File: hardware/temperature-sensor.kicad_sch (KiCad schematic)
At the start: 35 parts, among them J1 USB_B, J2 Barrel_Jack, J3 Conn_01x02_Pin, J4 Conn_01x03, SW1 SW_Push, U1 MCP2221AxP, U2 MCP1702-3302E, U3 ESP-01v090, U4 AHT10

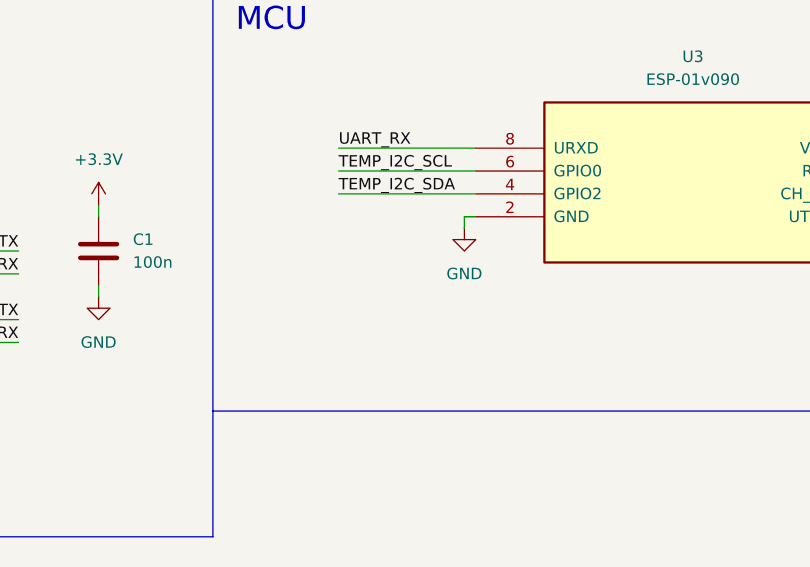
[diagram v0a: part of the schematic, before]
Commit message: Rev 0.2 - Added jumper to support UART boot
Signed-off-by: Matthew <mnickson@sidingsmedia.com>
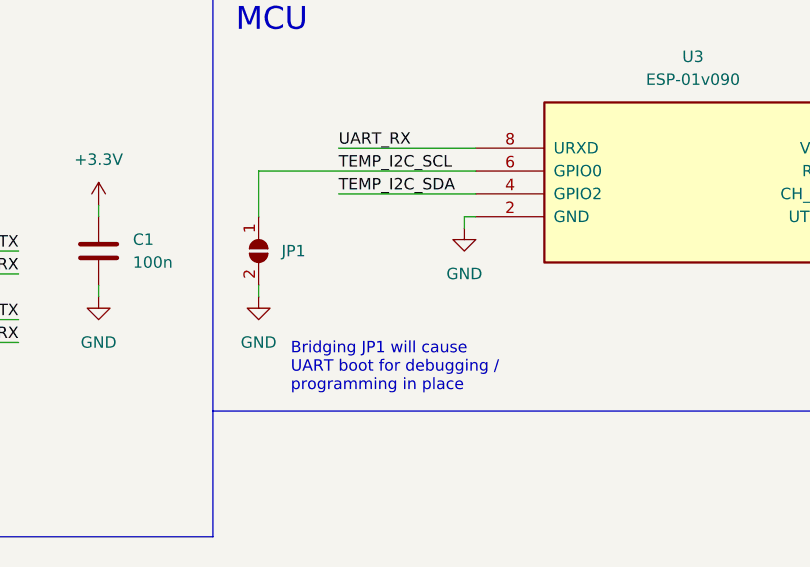
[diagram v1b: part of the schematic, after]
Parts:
- added JP1: SolderJumper_2_Open, Jumper:SolderJumper-2_P1.3mm_Open_Pad1.0x1.5mm, symbol Jumper:SolderJumper_2_Open
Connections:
- net GND: now also JP1.2 (B)
- net TEMP_I2C_SCL: now also JP1.1 (A)
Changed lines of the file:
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@@
   (title_block
     (title "Temperature Sensor")
-    (date "2024-01-07")
-    (rev "0.1")
+    (date "2024-01-13")
+    (rev "0.2")
     (company "Sidings Media")
     (comment 1 "Licence: CERN-OHL-P-2.0 or any later version")
@@
     (stroke (width 0) (type default))
   )
+  (wire (pts (xy 95.25 132.08) (xy 95.25 133.35))
+    (stroke (width 0) (type default))
+  )
   (wire (pts (xy 140.97 85.09) (xy 140.97 86.36))
     (stroke (width 0) (type default))
@@
     (stroke (width 0) (type default))
   )
-  (wire (pts (xy 104.14 119.38) (xy 119.38 119.38))
+  (wire (pts (xy 95.25 119.38) (xy 119.38 119.38))
     (stroke (width 0) (type default))
   )
@@
     (stroke (width 0) (type default))
   )
+  (wire (pts (xy 95.25 124.46) (xy 95.25 119.38))
+    (stroke (width 0) (type default))
+  )
   (wire (pts (xy 257.81 25.4) (xy 257.81 26.67))
     (stroke (width 0) (type default))
@@
   (wire (pts (xy 257.81 48.26) (xy 257.81 46.99))
     (stroke (width 0) (type default))
+  )
+  (text_box "Bridging JP1 will cause UART boot for debugging / programming in place"
+    (at 97.79 137.16 0) (size 30.48 7.62)
+    (stroke (width -0.0001) (type default))
+    (fill (type none))
+    (effects (font (size 1.27 1.27)) (justify left top))
   )
   (text "Debug UART" (at 238.76 62.23 0)
@@
     )
   )
+  (symbol (lib_id "Jumper:SolderJumper_2_Open") (at 95.25 128.27 270) (unit 1)
+    (in_bom yes) (on_board yes) (dnp no) (fields_autoplaced)
+    (property "Reference" "JP1" (at 97.79 128.27 90)
+      (effects (font (size 1.27 1.27)) (justify left))
+    )
+    (property "Value" "SolderJumper_2_Open" (at 99.06 128.27 0)
+      (effects (font (size 1.27 1.27)) hide)
+    )
+    (property "Footprint" "Jumper:SolderJumper-2_P1.3mm_Open_Pad1.0x1.5mm" (at 95.25 128.27 0)
+      (effects (font (size 1.27 1.27)) hide)
+    )
+    (property "Datasheet" "~" (at 95.25 128.27 0)
+      (effects (font (size 1.27 1.27)) hide)
+    )
+    (pin "2")
+    (pin "1")
+    (instances
+      (project "temperature-sensor"
+        (path "/dee5b369-e034-4202-bd61-980b6f64eea9"
+          (reference "JP1") (unit 1)
+        )
+      )
+    )
+  )
   (symbol (lib_id "power:+3.3V") (at 170.18 26.67 0) (unit 1)
     (in_bom yes) (on_board yes) (dnp no) (fields_autoplaced)
@@
         )
       )
+    )
+  )
+  (symbol (lib_id "power:GND") (at 95.25 133.35 0) (unit 1)
+    (in_bom yes) (on_board yes) (dnp no) (fields_autoplaced)
+    (property "Reference" "#PWR022" (at 95.25 139.7 0)
+      (effects (font (size 1.27 1.27)) hide)
+    )
+    (property "Value" "GND" (at 95.25 138.43 0)
+      (effects (font (size 1.27 1.27)))
+    )
+    (property "Footprint" "" (at 95.25 133.35 0)
+      (effects (font (size 1.27 1.27)) hide)
+    )
+    (property "Datasheet" "" (at 95.25 133.35 0)
+      (effects (font (size 1.27 1.27)) hide)
+    )
+    (pin "1")
+    (instances
+      (project "temperature-sensor"
+        (path "/dee5b369-e034-4202-bd61-980b6f64eea9"
+          (reference "#PWR022") (unit 1)
+        )
+      )

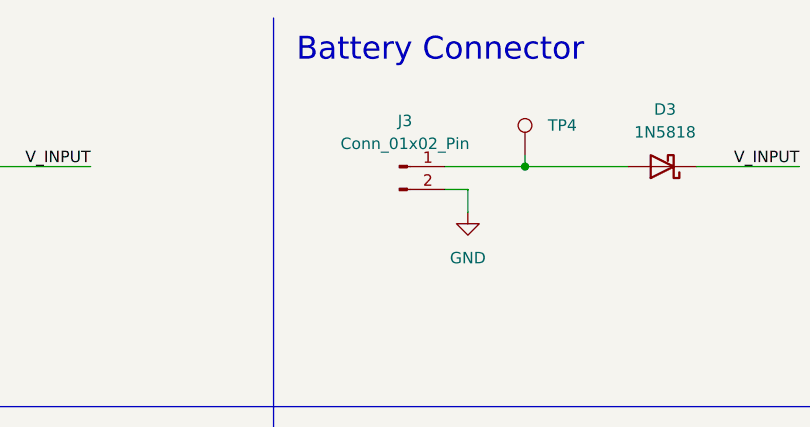
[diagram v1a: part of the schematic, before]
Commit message: Fixed fab references
Signed-off-by: Matthew <mnickson@sidingsmedia.com>
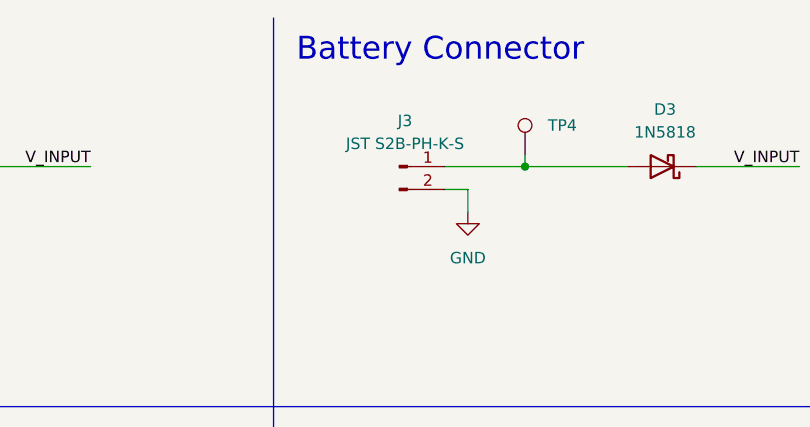
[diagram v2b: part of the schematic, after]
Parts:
- J3: value Conn_01x02_Pin -> JST S2B-PH-K-S
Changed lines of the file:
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@@
       (effects (font (size 1.27 1.27)))
     )
-    (property "Value" "Conn_01x02_Pin" (at 104.775 26.67 0)
+    (property "Value" "JST S2B-PH-K-S" (at 104.775 26.67 0)
       (effects (font (size 1.27 1.27)))
     )
